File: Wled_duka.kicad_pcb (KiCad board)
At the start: 2 copper layers, 100 x 100 mm, 47 parts, among them J1 7775-2, J2 DATA channels, J3 CH1&2, J4 CH3&4, J5 Relay out, J6 DMX512, J7 7775-2, J8 Vin_alt, Q1 DMN3067L-7, U1 ADM3485xR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

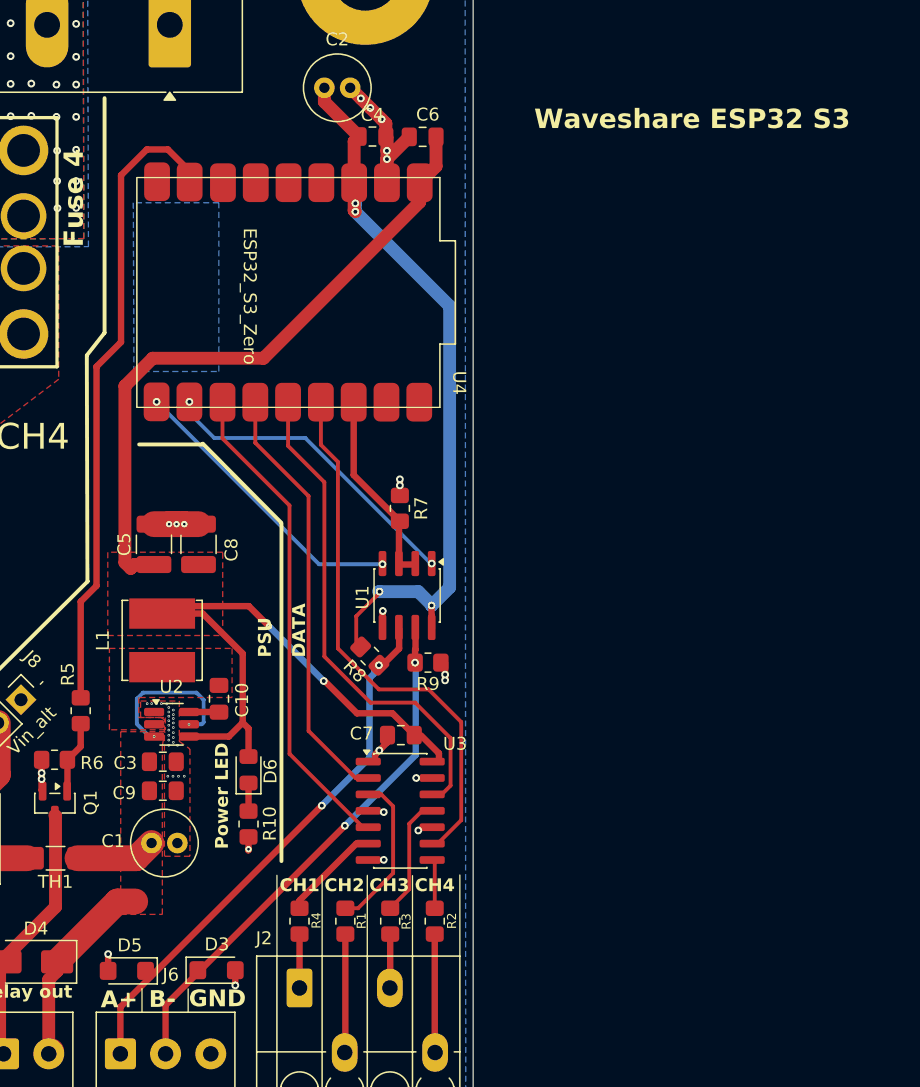
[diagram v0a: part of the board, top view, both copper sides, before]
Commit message: 5V CAP + High current trace
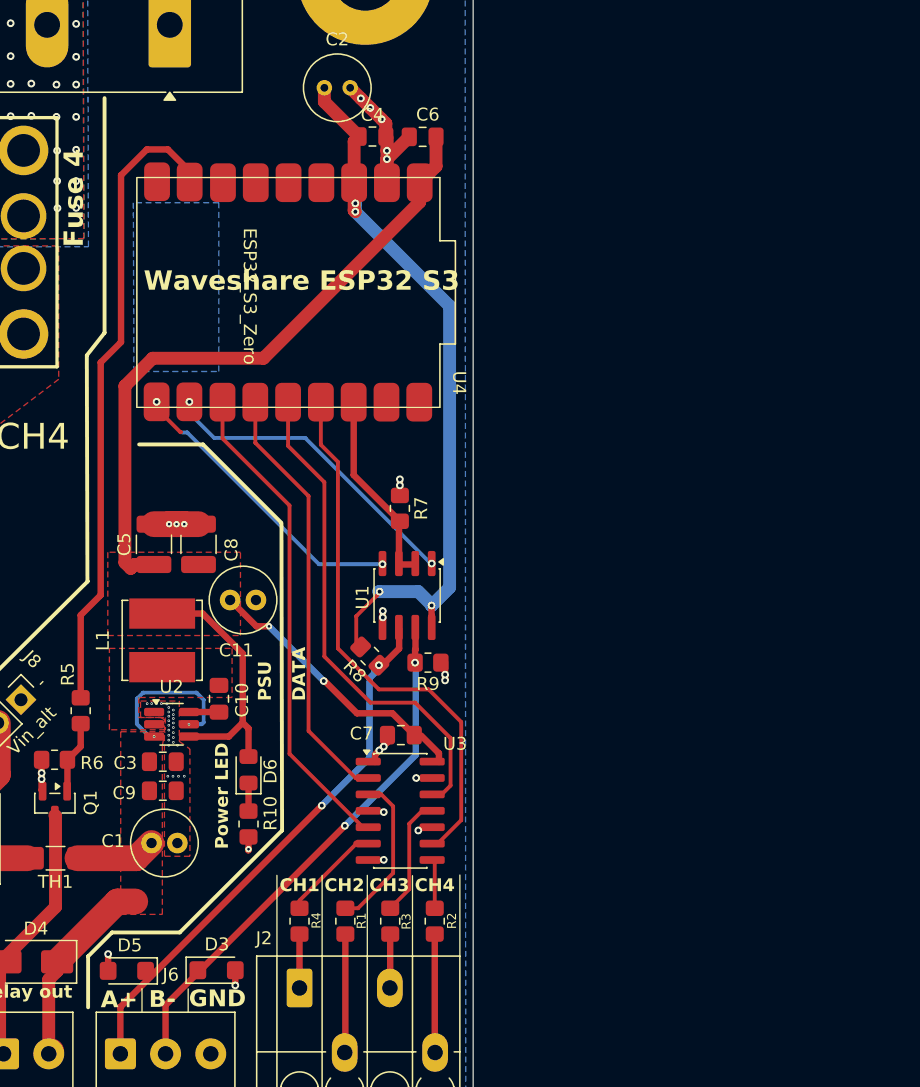
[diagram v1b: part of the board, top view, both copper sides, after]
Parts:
- added C11: 100uF, Capacitor_THT:C_Radial_D5.0mm_H11.0mm_P2.00mm, F.Cu at (147.8, 115.2)
- C2: value 100uF -> 47uF; footprint Capacitor_THT:C_Radial_D5.0mm_H11.0mm_P2.00mm -> Capacitor_THT:C_Radial_D5.0mm_H7.0mm_P2.00mm
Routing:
- net +5V: track 99.9 -> 95.9 mm
- net GND: vias 50 -> 52
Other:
- board text removed: "<----HIBÁS lábkiosztás!!!!!"

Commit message: Merge branch 'main' of github.com:regamp/Wled-controler-with-DMX
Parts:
- moved R5 11.0 mm to (131.3, 133.7), turned to 0 degrees
- moved R6 8.70 mm to (131.3, 135.8)
- moved Q1 8.70 mm to (131.3, 139.1)
- moved D2 3.90 mm to (130.5, 129.5), turned to 180 degrees
- moved TH1 2.65 mm to (136.6, 133.9)
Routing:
- net REL: track 49.4 -> 63.6 mm
- net Net-(D4-A): track 20.4 -> 10.7 mm
- net V12: track 34.0 -> 31.4 mm
- net Net-(D2-K): track 3.78 -> 5.29 mm
- net Vin: track 38.8 -> 37.6 mm
- net Net-(Q1-G): track 5.66 -> 4.56 mm
- net DI TX: track 22.9 -> 23.6 mm
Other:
- board text added: "500mA Fuse"
- board text added: "5V conv."
- board text added: "DMX"
- board text added: "Level shifter"
- board text added: "RX"
- board text added: "Rel"
- board text added: "TX"

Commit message: text fix
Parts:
- moved C11 0.25 mm to (148.0, 115.2)
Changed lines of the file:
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@@
 	(footprint "Capacitor_THT:C_Radial_D5.0mm_H11.0mm_P2.00mm"
 		(layer "F.Cu")
-		(at 147.775 115.2)
+		(at 148.025 115.25)
 		(descr "C, Radial series, Radial, pin pitch=2.00mm, diameter=5mm, height=11mm, Non-Polar Electrolytic Capacitor")
 		(tags "C Radial series Radial pin pitch 2.00mm diameter 5mm height 11mm Non-Polar Electrolytic Capacitor")
@@
 		(tags "Connector")
 		(property "Reference" "J7"
-			(at 2.375 -3.505 0)
+			(at 8.7 -3.425 0)
 			(layer "F.SilkS")
 			(effects
@@
 		(tags "Connector")
 		(property "Reference" "J1"
-			(at 2.375 -3.505 0)
+			(at 8.875 -3.435 0)
 			(layer "F.SilkS")
 			(effects
@@
 	)
 	(segment
-		(start 154.525 103.575)
+		(start 151.375 103.575)
 		(end 147.275 103.575)
 		(width 0.3)
@@
 	)
 	(segment
-		(start 163.3875 112.375)
-		(end 163.5 112.2625)
+		(start 161.325 110.375)
+		(end 158.175 110.375)
 		(width 0.3)
 		(layer "B.Cu")
@@
 	)
 	(segment
+		(start 163.3875 112.375)
+		(end 163.5 112.2625)
+		(width 0.3)
+		(layer "B.Cu")
+		(net "RO RX")
+	)
+	(segment
 		(start 163.2125 112.2625)
-		(end 154.525 103.575)
+		(end 161.325 110.375)
+		(width 0.3)
+		(layer "B.Cu")
+		(net "RO RX")
+	)
+	(segment
+		(start 158.175 110.375)
+		(end 151.375 103.575)
 		(width 0.3)
 		(layer "B.Cu")
